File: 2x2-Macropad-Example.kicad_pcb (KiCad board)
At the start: 2 copper layers, 73 x 38.1 mm, 24 parts, among them SW1 SW_Push, U1 ATmega32U4-A, Y1 16MHz

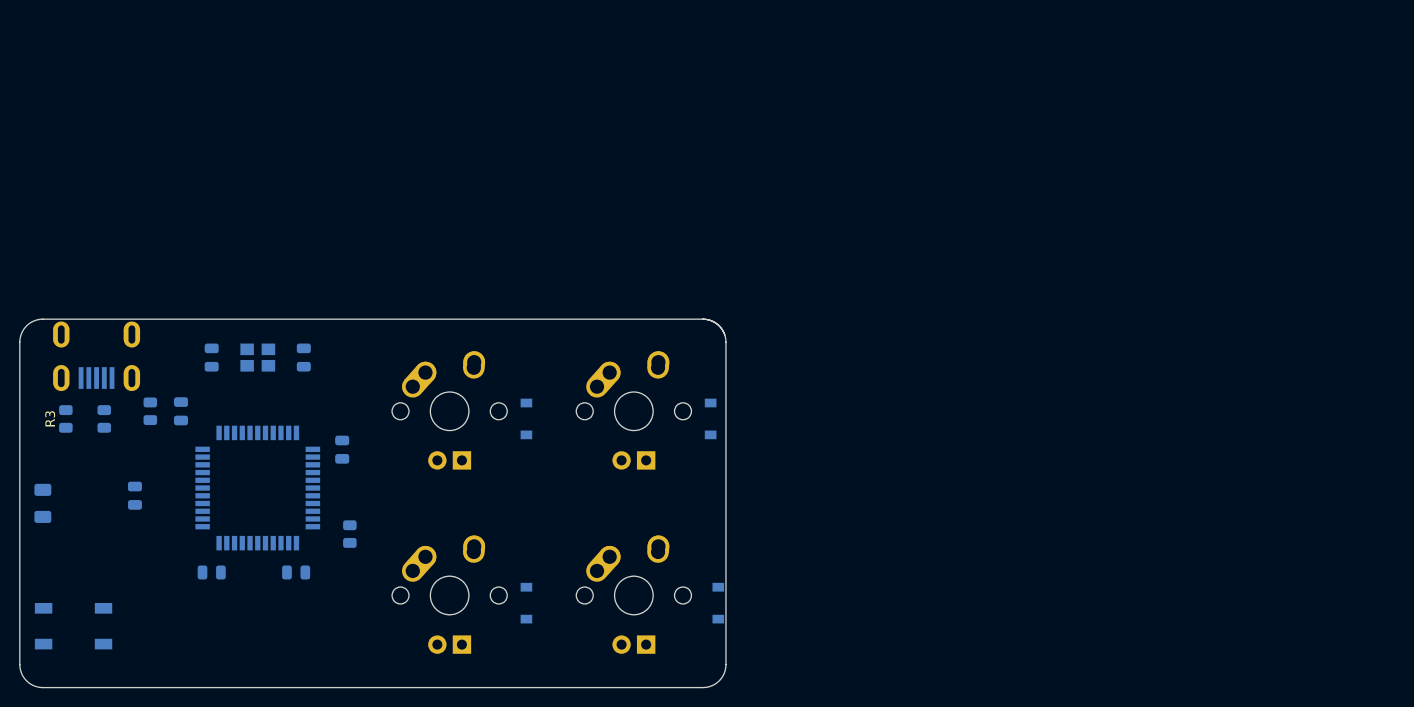
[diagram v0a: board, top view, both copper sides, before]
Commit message: mostly finished routing the traces
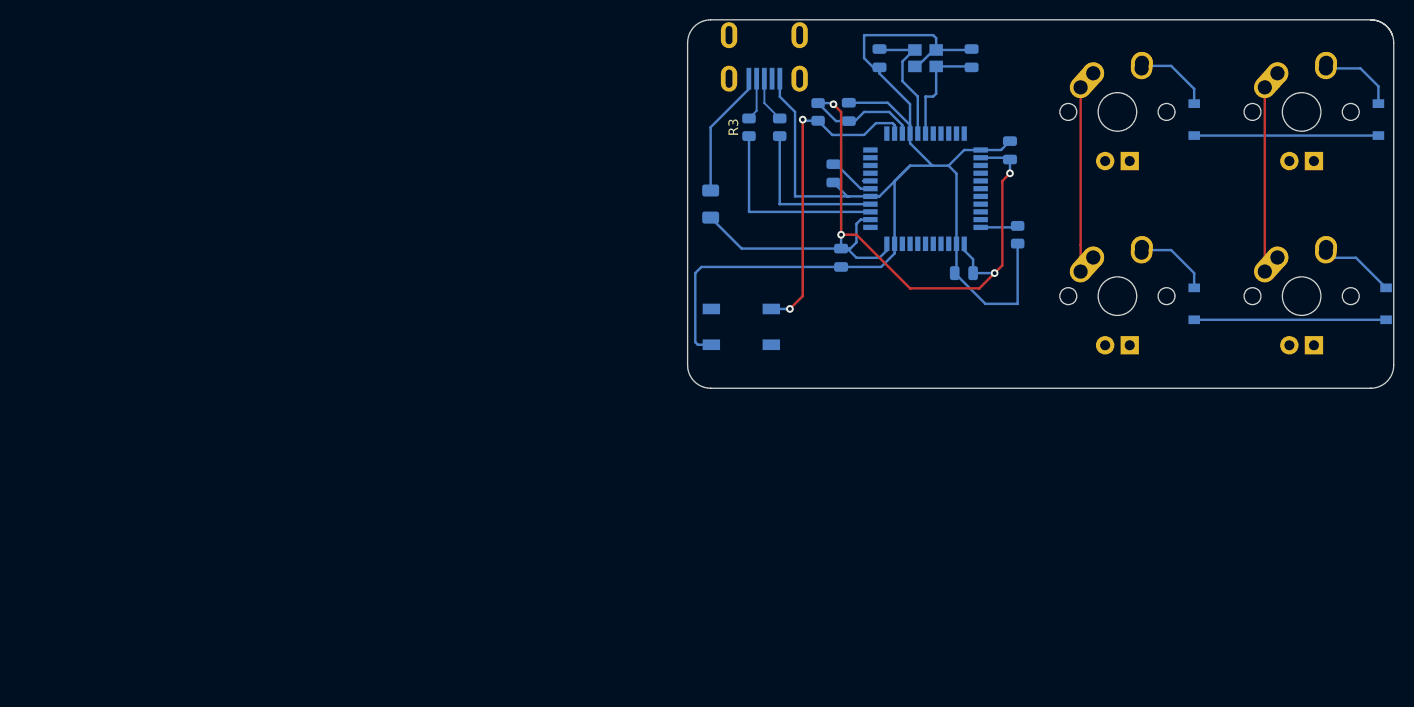
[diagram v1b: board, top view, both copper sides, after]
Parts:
- moved C1 84.5 mm to (127.8, 88.1), turned to -90 degrees
- moved C3 79.6 mm to (113.5, 100.0)
- moved R3 76.8 mm to (104.8, 95.2)
- moved R2 76.1 mm to (108.0, 95.2)
- moved C4 75.7 mm to (115.1, 93.7)
- moved D3 75.7 mm to (150.8, 113.5)
- moved D4 75.7 mm to (170.7, 113.5)
- moved F1 75.7 mm to (100.8, 103.2)
- moved MX1 75.7 mm to (142.9, 93.7)
- moved MX2 75.7 mm to (161.9, 93.7)
- moved R1 75.7 mm to (111.9, 93.7), turned to -90 degrees
- moved U1 75.7 mm to (123.0, 101.6)
- moved USB1 75.7 mm to (106.4, 85.7)
- moved C5 75.7 mm to (131.8, 97.6)
- moved C6 75.7 mm to (127.0, 110.3)
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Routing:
- net GND: track 0.00 -> 145.8 mm
- net +5V: track 0.00 -> 95.5 mm, vias 0 -> 4
- net Net-(R1-Pad2): track 0.00 -> 34.1 mm, vias 0 -> 2
- net Net-(R3-Pad2): track 0.00 -> 20.4 mm
- net ROW1: track 0.00 -> 19.8 mm
- net ROW0: track 0.00 -> 19.1 mm
- net COL1: track 0.00 -> 19.0 mm
- net COL0: track 0.00 -> 19.0 mm
- net Net-(R2-Pad2): track 0.00 -> 16.4 mm
- net Net-(C2-Pad2): track 0.00 -> 13.6 mm
- net VCC: track 0.00 -> 13.2 mm
- net Net-(C1-Pad2): track 0.00 -> 11.6 mm
- net Net-(D3-Pad2): track 0.00 -> 8.06 mm
- net Net-(D1-Pad2): track 0.00 -> 8.06 mm
- net Net-(D2-Pad2): track 0.00 -> 8.00 mm
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
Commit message: finished routing and laying fills, DRC issue with usb and mx footprints
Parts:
- moved D4 0.79 mm to (169.9, 113.5)
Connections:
- U1 pad 27: unconnected-(U1-Pad27) -> ROW0
- U1 pad 28: unconnected-(U1-Pad28) -> COL1
- U1 pad 29: unconnected-(U1-Pad29) -> COL0
- U1 pad 30: unconnected-(U1-Pad30) -> ROW1
- USB1 pad 6: unconnected-(USB1-Pad6) -> GND
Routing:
- net COL1: track 19.0 -> 52.0 mm
- net ROW1: track 19.8 -> 52.1 mm
- net ROW0: track 19.1 -> 46.0 mm
- net COL0: track 19.0 -> 34.3 mm
- net +5V: track 95.5 -> 99.7 mm, vias 4 -> 5
- added copper zone on B.Cu, net GND
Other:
- outline, holes or cut-outs redrawn
